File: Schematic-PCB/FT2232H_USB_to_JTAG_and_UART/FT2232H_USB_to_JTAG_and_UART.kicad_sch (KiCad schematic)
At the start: 8 parts, among them J1 TI_JTAG14 Connector, J2 Conn_01x04_Pin, U2 ISO7761, U3 ISO7221, U4 SN74ALVC244

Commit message: Updated Kicad project, added PCB layout PDF files and FT2232H XML file
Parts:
- added D1: LED Blue, LED_THT:LED_D5.0mm, symbol Device:LED
- added D2: LED Green, LED_THT:LED_D5.0mm, symbol Device:LED
- added D3: LED Red, LED_THT:LED_D5.0mm, symbol Device:LED
- added D4: LED Yellow, LED_THT:LED_D5.0mm, symbol Device:LED
- added R3, R4, R5: 1K, Resistor_THT:R_Axial_DIN0207_L6.3mm_D2.5mm_P10.16mm_Horizontal, symbol Device:R
- added R6: 500, Resistor_THT:R_Axial_DIN0207_L6.3mm_D2.5mm_P10.16mm_Horizontal, symbol Device:R
- U1: value ~ -> FT2232H
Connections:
- net UART_GND is gone; now on net MCU_GND: J2.4 (Pin_4), U3.5 (Gnd2)
- net UART_VCC is gone; now on net MCU_VCC: J2.1 (Pin_1), U3.8 (Vcc2)
- net +3.3V: now also D4.2 (A)
- net GND1: now also R5.1, R6.2
- net RX_LED: now also R4.1
- net TX_LED: now also R3.1
- net VBUS: now also D1.2 (A), D2.2 (A), D3.2 (A)
- new net: D2.1 (K), R4.2
- new net: D4.1 (K), R6.1
- new net: D3.1 (K), R5.2
- new net: D1.1 (K), R3.2
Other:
- note added: "Buffer"
- note added: "Connectors"
- note added: "Digital Isolators"
- note added: "FT2232H Mini Module"
- note added: "Power Indicator LEDs"
- note added: "UART Status LEDs"
- moved on the sheet: J1, J2, U2, U3

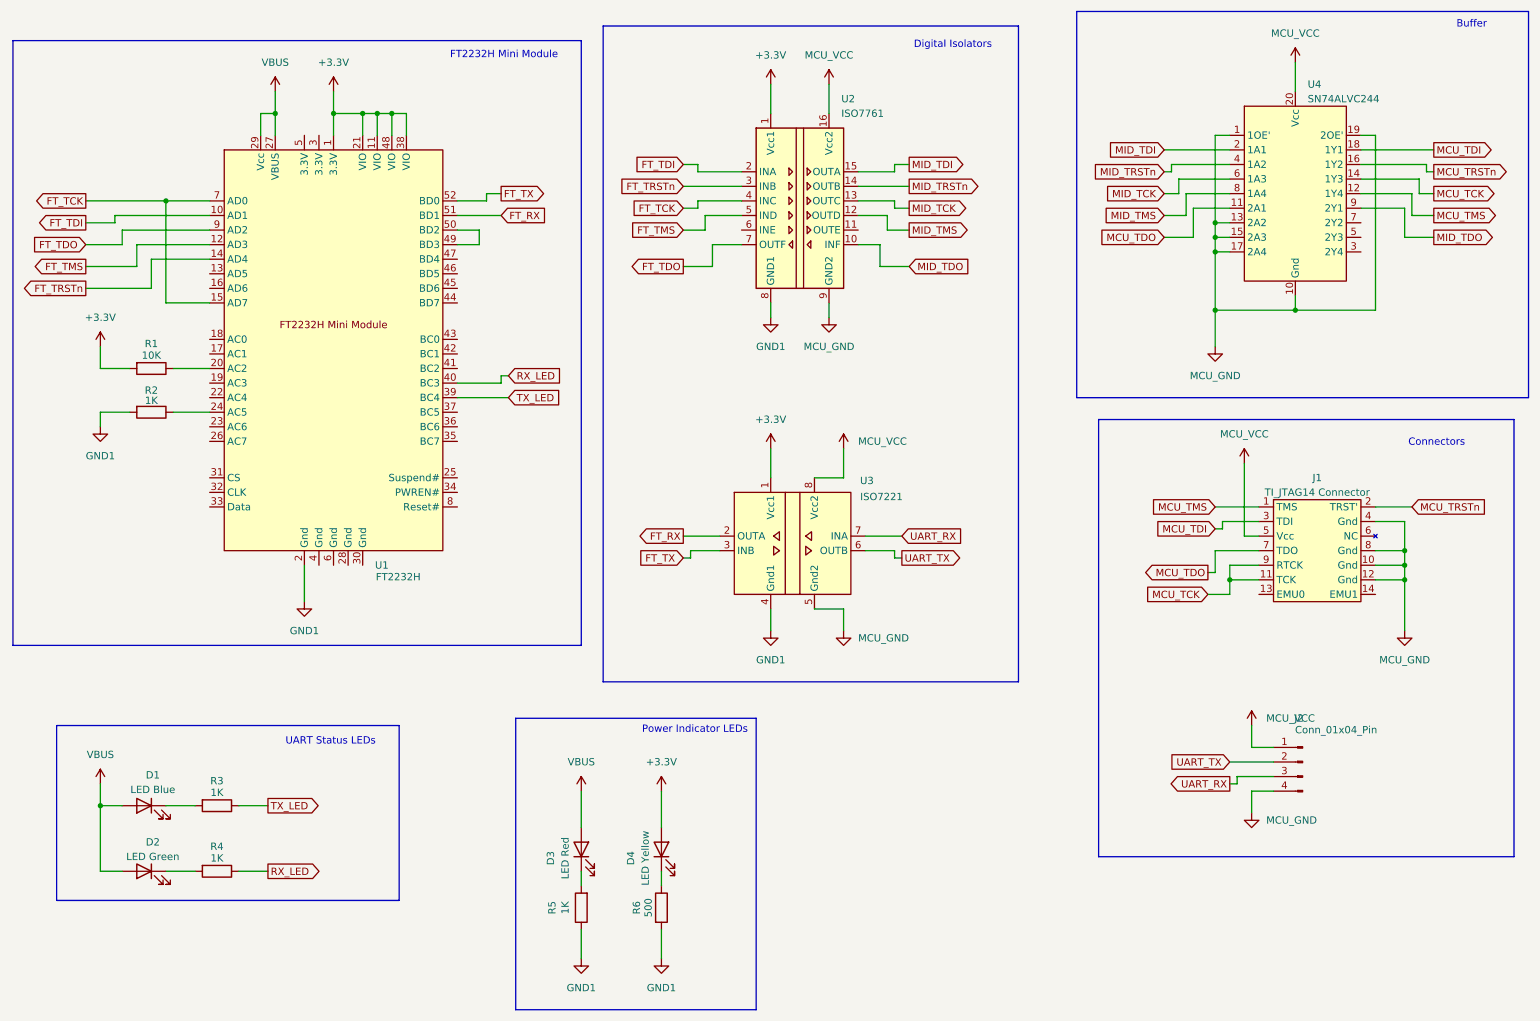
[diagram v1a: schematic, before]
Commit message: Removed buffer IC from schematic
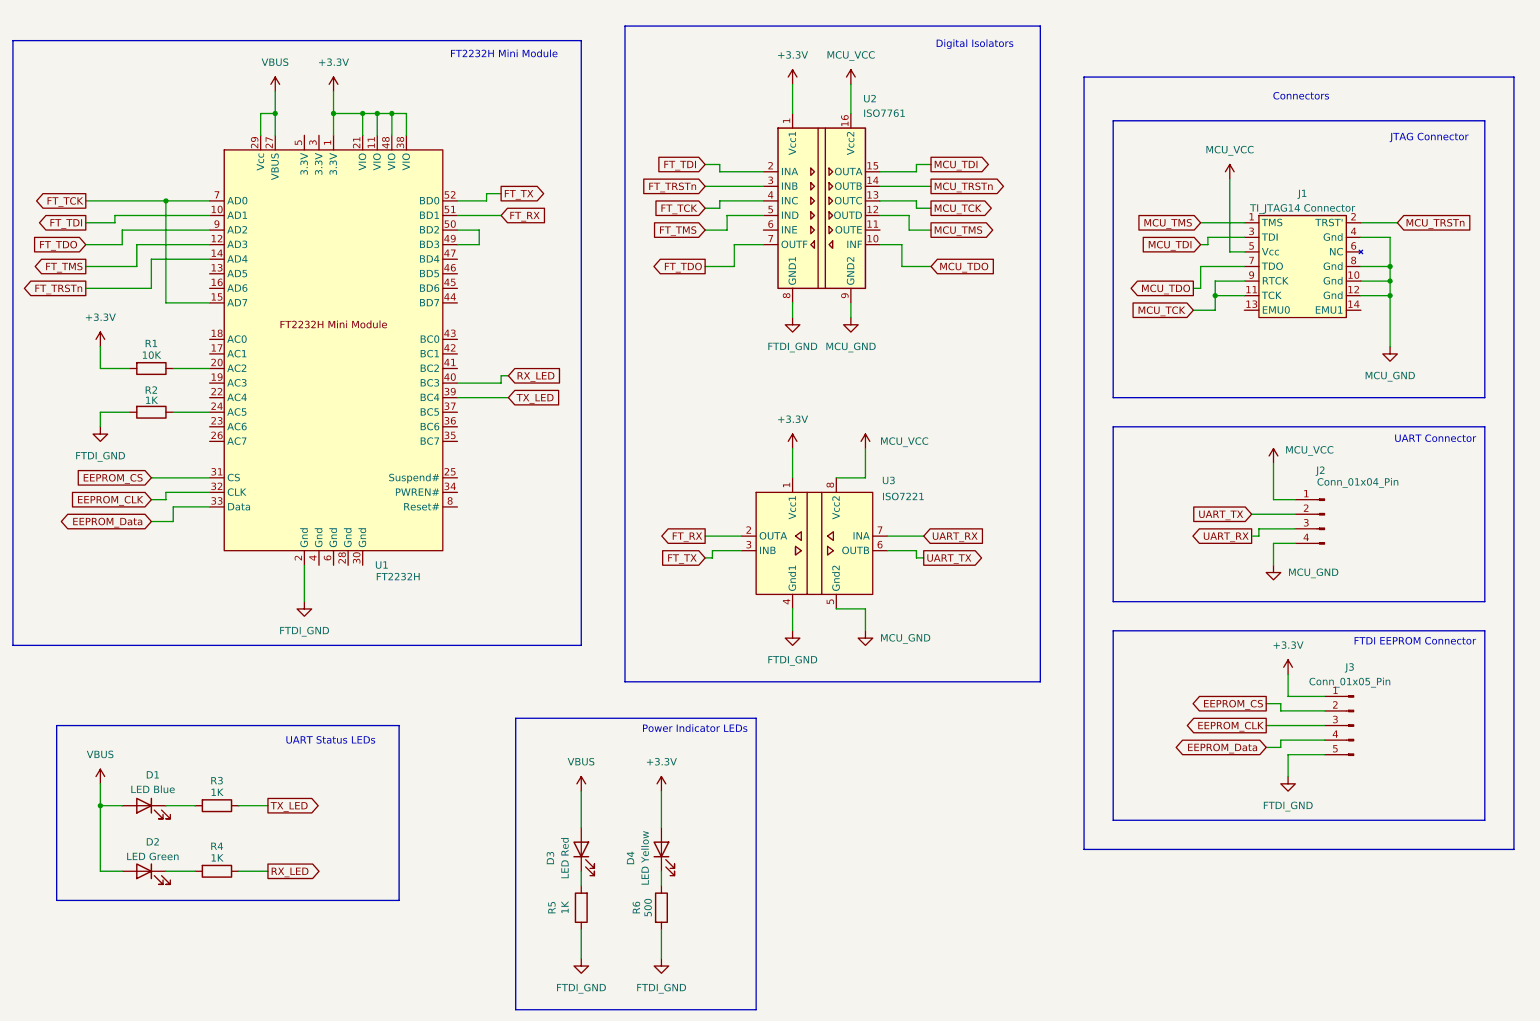
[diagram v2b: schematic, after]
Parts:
- removed U4: SN74ALVC244, SOIC-DIP:SOIC_20-DIP, symbol SN74ALVC244:SN74ALVC244
- added J3: Conn_01x05_Pin, Connector_PinHeader_2.54mm:PinHeader_1x05_P2.54mm_Vertical, symbol Connector:Conn_01x05_Pin
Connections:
- net MID_TCK is gone; now on net MCU_TCK: U2.13 (OUTC)
- net MID_TDI is gone; now on net MCU_TDI: U2.15 (OUTA)
- net MID_TDO is gone; now on net MCU_TDO: U2.10 (INF)
- net MID_TMS is gone; now on net MCU_TMS: U2.12 (OUTD)
- net MID_TRSTn is gone; now on net MCU_TRSTn: U2.14 (OUTB)
- net +3.3V: now also J3.1 (Pin_1)
- net EEPROM_CS: now reaches U1.31 (CS)
- net EEPROM_CS: now also J3.2 (Pin_2)
- net EEPROM_CLK: now reaches U1.32 (CLK)
- net EEPROM_CLK: now also J3.3 (Pin_3)
- net EEPROM_Data: now reaches U1.33 (Data)
- net EEPROM_Data: now also J3.4 (Pin_4)
- net GND1 renamed FTDI_GND
- net FTDI_GND: now also J3.5 (Pin_5)
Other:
- note added: "FTDI EEPROM Connector"
- note added: "JTAG Connector"
- note added: "UART Connector"
- note removed: "Buffer"
- moved on the sheet: J1, J2, U2, U3

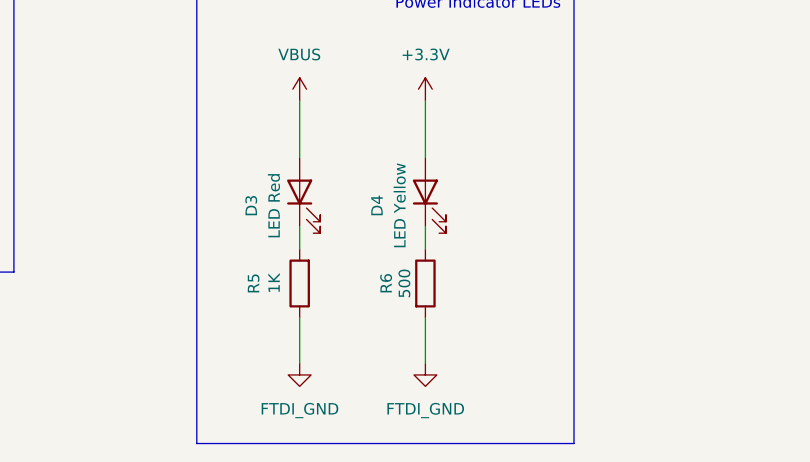
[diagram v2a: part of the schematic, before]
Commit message: Changed a resistor value
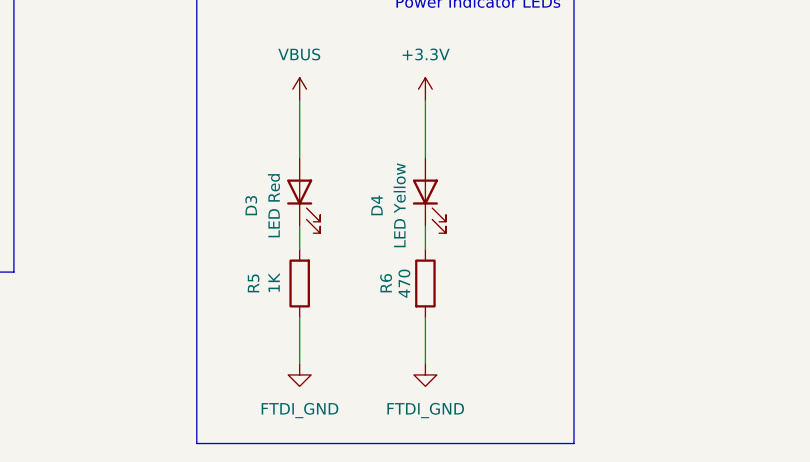
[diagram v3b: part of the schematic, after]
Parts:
- R6: value 500 -> 470
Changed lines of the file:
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@@
 			)
 		)
-		(property "Value" "500"
+		(property "Value" "470"
 			(at 125.984 172.72 90)
 			(effects
